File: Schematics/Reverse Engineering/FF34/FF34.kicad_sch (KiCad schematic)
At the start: 146 parts, among them J1 Conn_01x40, Q1 Q_PNP_EBC, Q10 Q_PNP_EBC, Q11 Q_PNP_EBC, Q12 Q_PNP_EBC, Q13 Q_PNP_EBC, Q14 Q_PNP_EBC, Q15 Q_PNP_EBC, Q16 Q_PNP_EBC, Q17 Q_PNP_EBC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

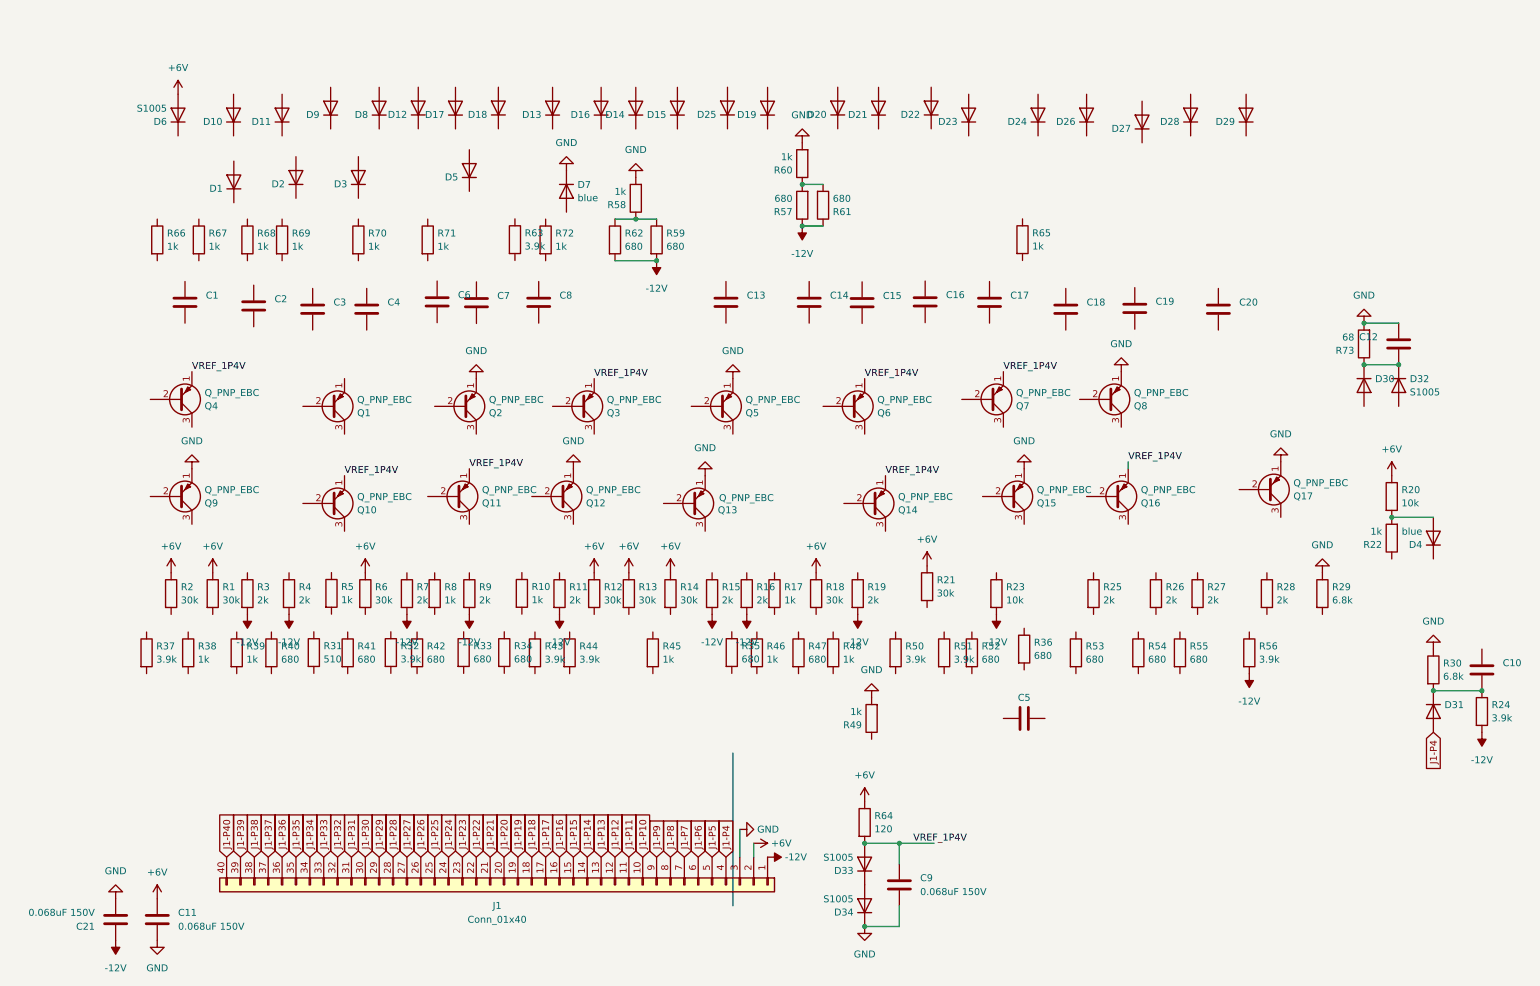
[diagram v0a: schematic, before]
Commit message: Almost done with the first FF gate
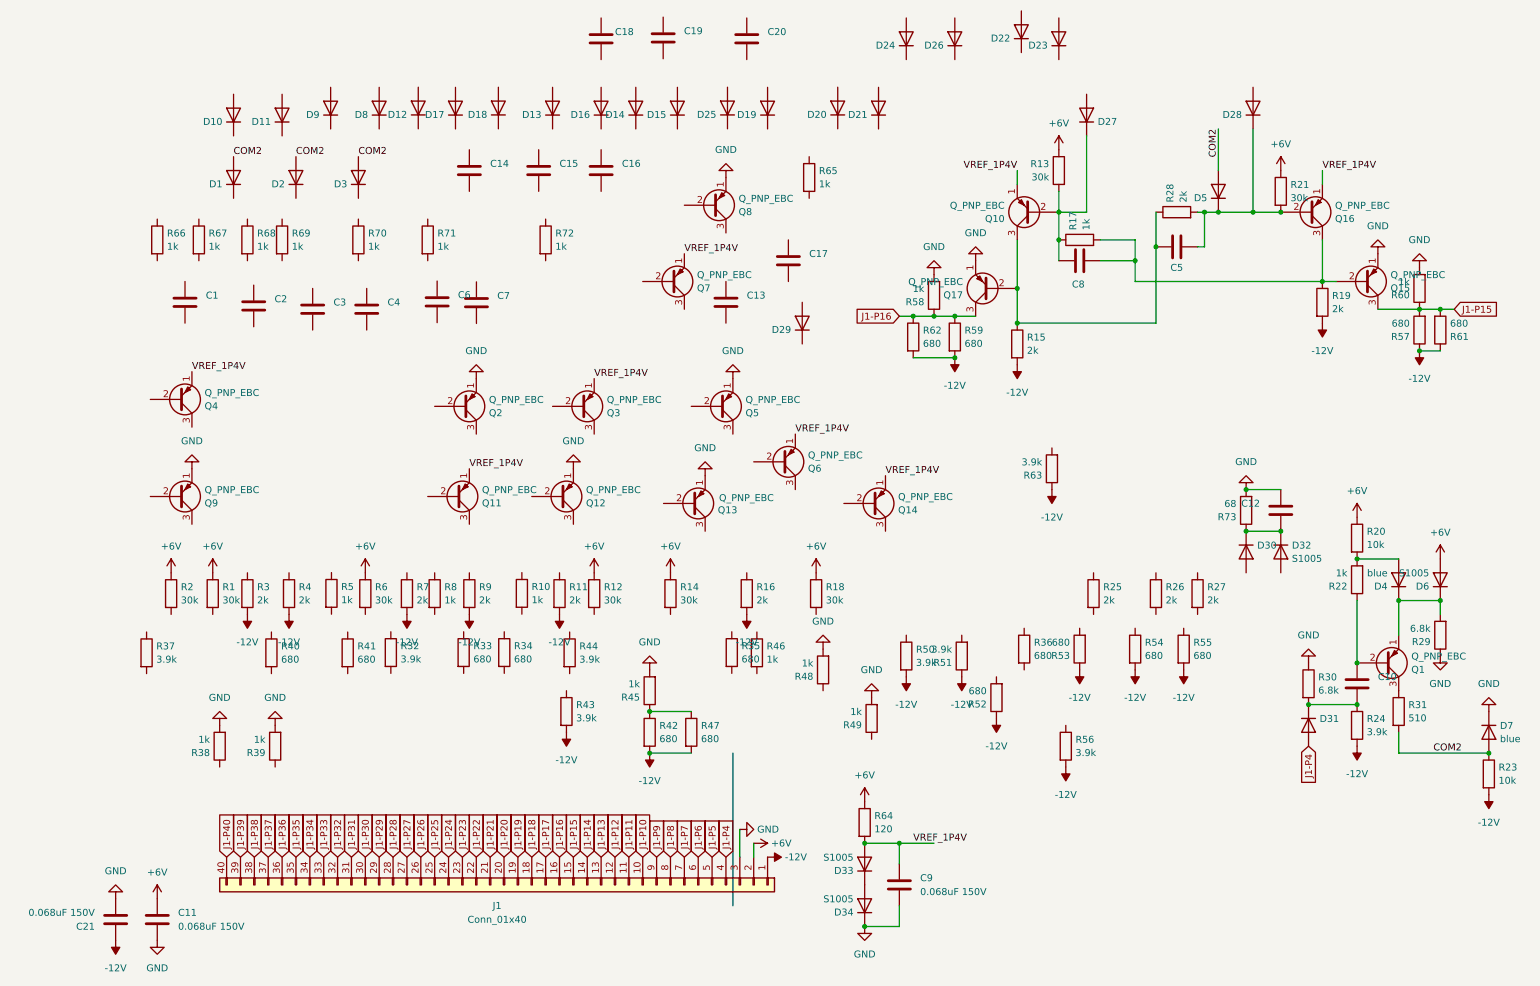
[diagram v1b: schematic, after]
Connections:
- net -12V: now also R42.2, R43.2, R47.2, R50.2, R51.1, R52.1, R53.1, R54.2, R55.2, R63.1
- net GND: now also R38.2, R39.2, R45.2, R48.2
- net J1-P15: now also Q15.3 (C), R57.2, R60.1, R61.2
- net J1-P16: now also Q17.3 (C), R58.1, R59.1, R62.1
- net at R21.2: now also C5.1, D28.1 (K), D5.1 (K), Q16.2 (B), R28.2
- net at C10.1: now also Q1.2 (B), R22.1
- net COM2: now reaches D7.2 (A)
- net COM2: now also D1.2 (A), D2.2 (A), D3.2 (A), D5.2 (A), R23.1, R31.2
- net at Q1.1 (E): now also D4.1 (K), D6.1 (K), R29.2
- net at Q1.3 (C): now also R31.1
- net at R47.1: now also R42.1, R45.1
- net at R19.1: now also C8.1, Q15.2 (B), Q16.3 (C), R17.2
- net at R17.1: now also C8.2, D27.1 (K), Q10.2 (B), R13.2
- net at C5.2: now also Q10.3 (C), Q17.2 (B), R15.1, R28.1
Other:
- moved on the sheet: C10, C12, C14, C15, C16, C17, C18, C19, C20, C5, C8, D1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
